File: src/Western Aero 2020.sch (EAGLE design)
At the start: 97 parts, among them IC1 LT1963AET, IC2 LT1963AET, J1 PITOT, J10 ANA_IO, J11 PWR, J2 BUZZER, J3 RX2/TX2, J4 RX3/TX3, J5 SPI, J6 DIG_IO, J7 RX1/TX1, J8 DIG_IO, J9 REF/GND, U3 TEENSY_3.5_DIL+4, U5 SPARKFUN_MPU9250_IMU, U6 ADAFRUIT_MPL3115A2_BAROMETER, U7 ADAFRUIT_INA219_BATTERY_SENSOR, U8 ADAFRUIT_RFM95W_LORA_RADIO, U9 ADAFRUIT_MTK3339_GPS

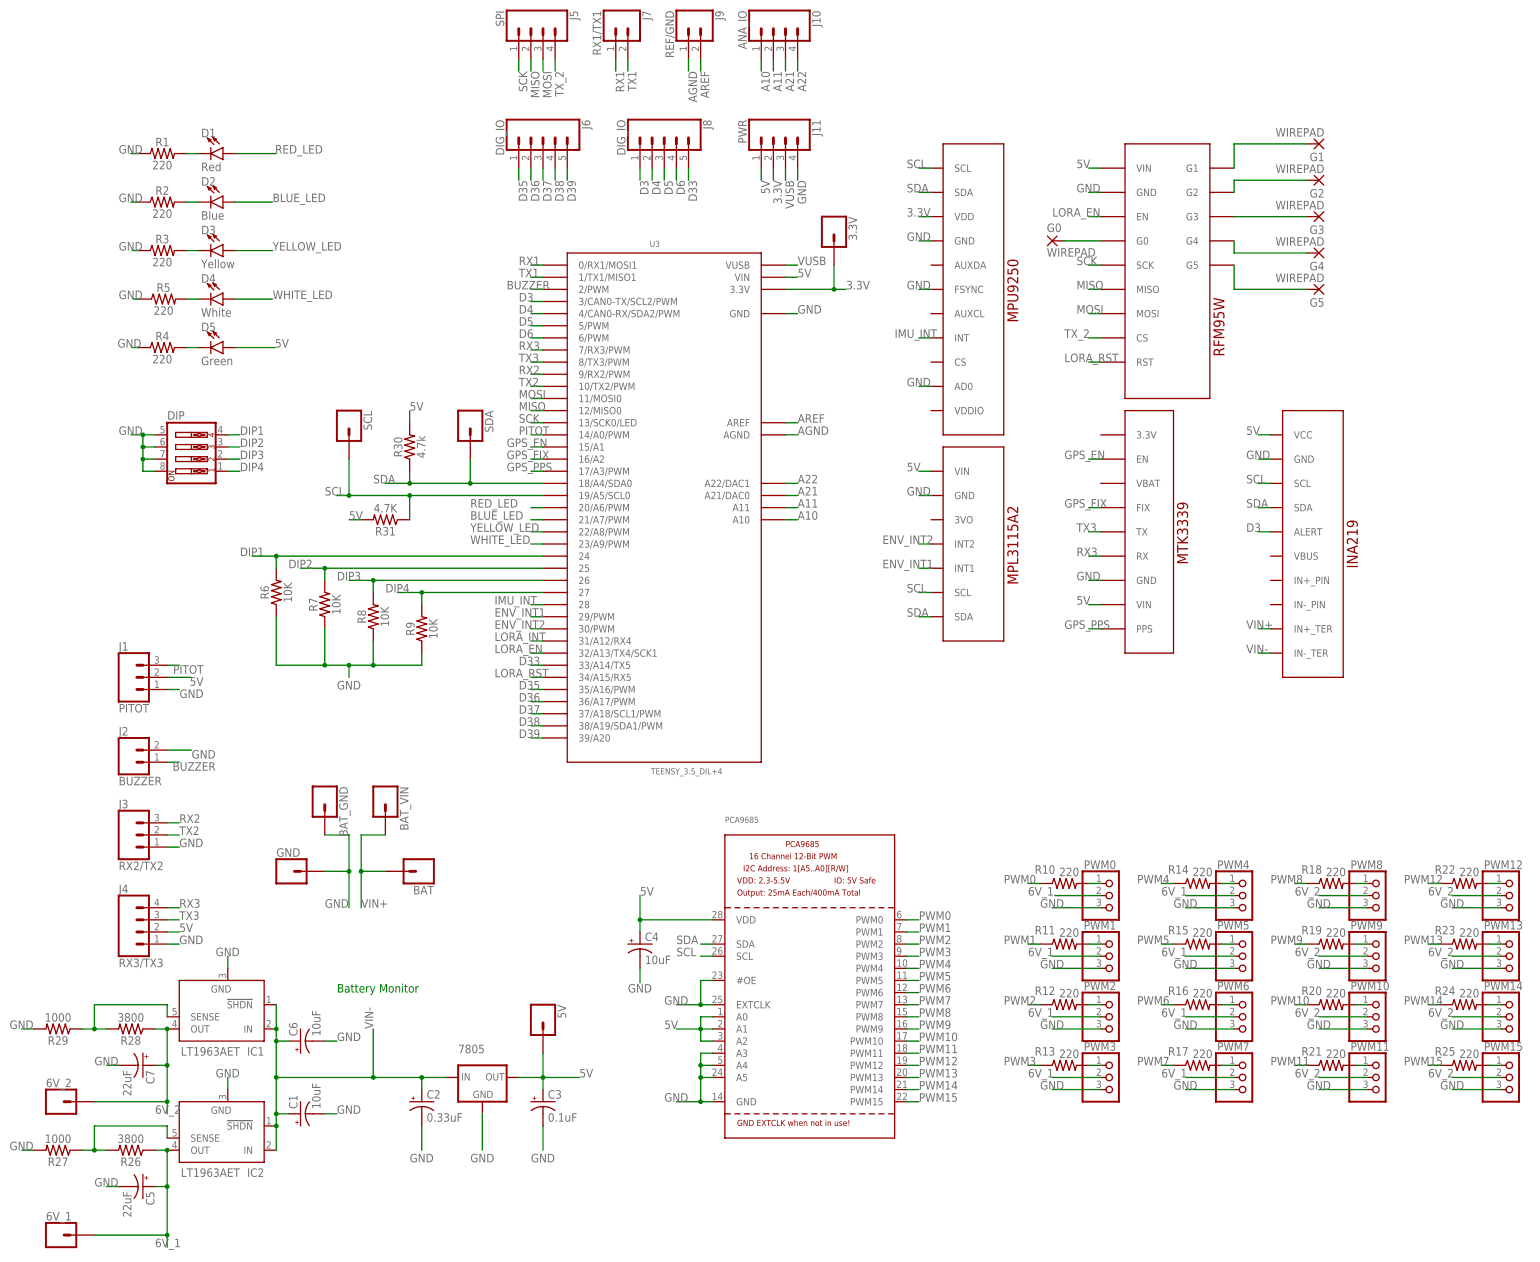
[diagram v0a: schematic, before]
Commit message: Remove battery monitor
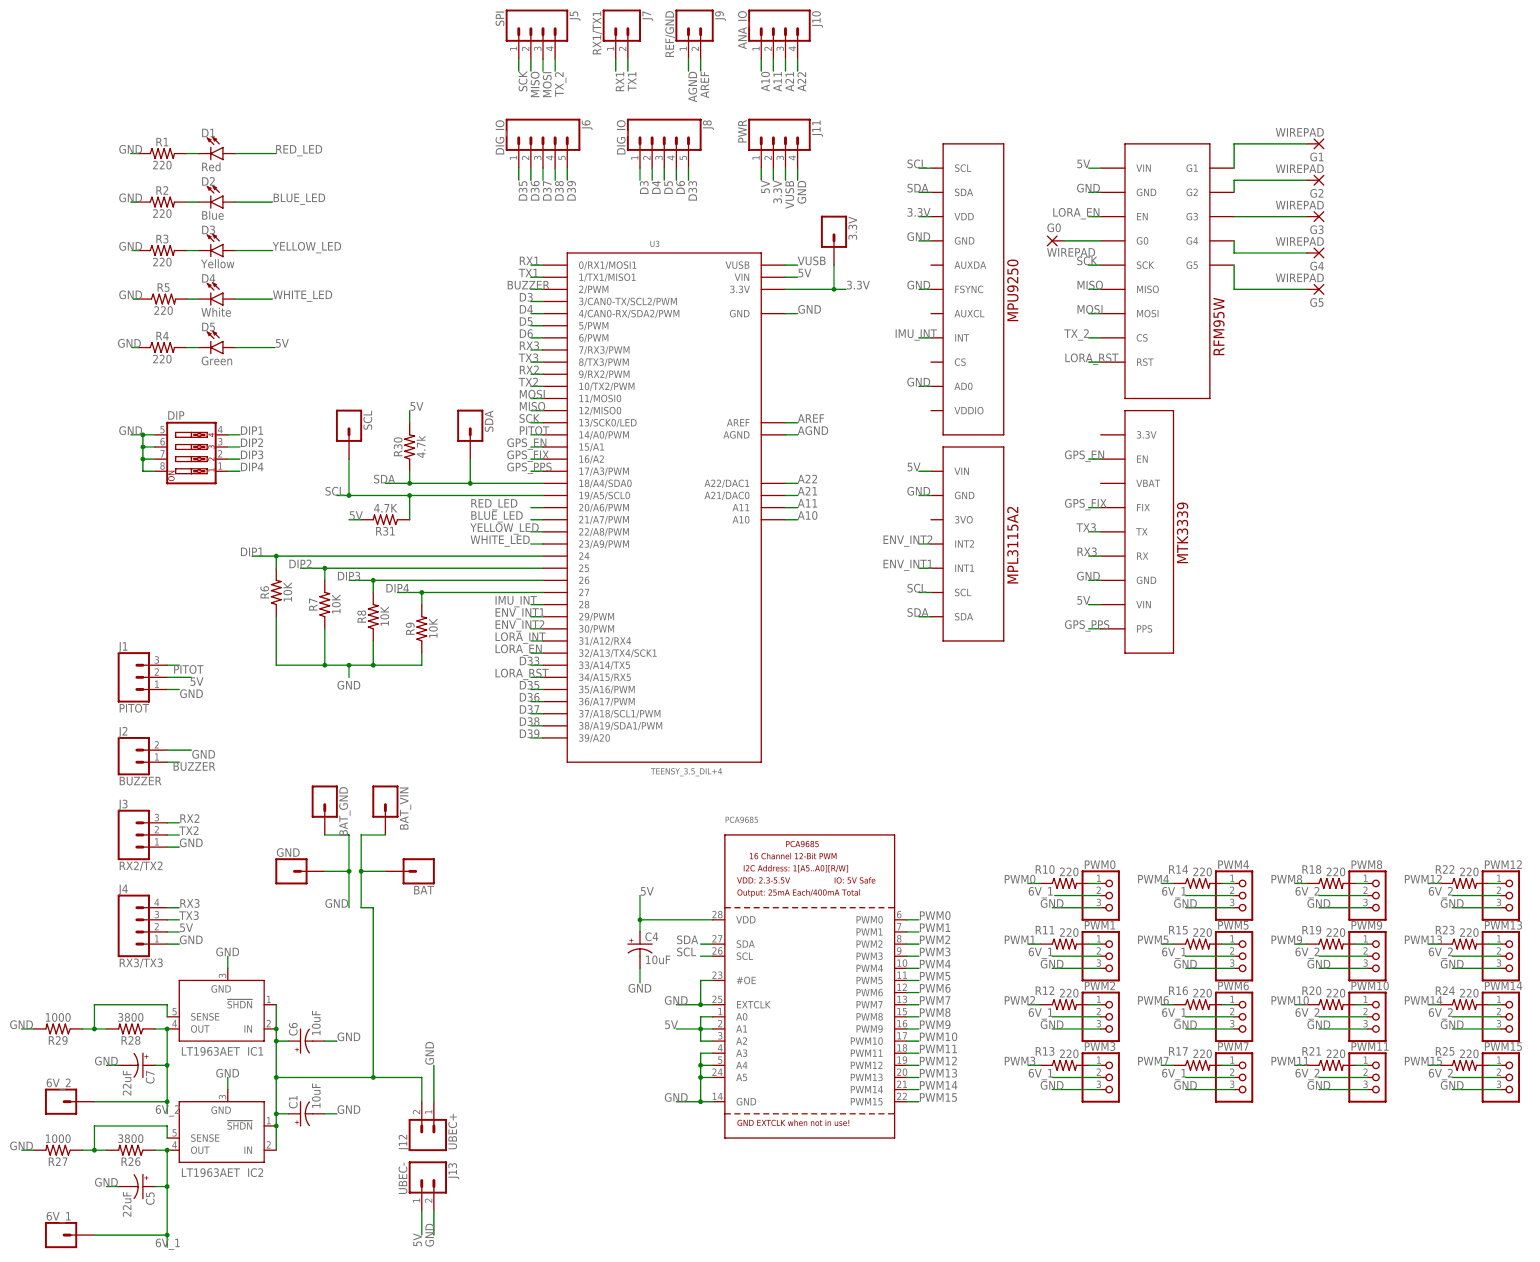
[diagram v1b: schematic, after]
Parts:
- removed 5V: (no value), SparkFun-Connectors:CONN_01
- removed 7805: 7805, SparkFun-IC-Power:V_REG_78XXSINK
- removed C2: 0.33uF, SparkFun-Capacitors:10UF-POLAR-RADIAL-2.5MM-25V-20%
- removed C3: 0.1uF, SparkFun-Capacitors:10UF-POLAR-RADIAL-2.5MM-25V-20%
- removed U7: ADAFRUIT_INA219_BATTERY_SENSOR, AERO_Eagle_Library:ADAFRUIT_INA219_BATTERY_SENSOR
- added J12: UBEC+, SparkFun-Connectors:CONN_02
- added J13: UBEC-, SparkFun-Connectors:CONN_02
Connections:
- removed net VIN+: BAT.1, BAT_VIN.1, U7.IN+_TER
- removed net VIN-: 7805.IN, C1.+, C2.+, C6.+, IC1.!SHDN, IC1.IN, IC2.!SHDN, IC2.IN, U7.IN-_TER
- new net BAT+: BAT.1, BAT_VIN.1, C1.+, C6.+, IC1.!SHDN, IC1.IN, IC2.!SHDN, IC2.IN, J12.2
- net 5V: now also J13.1; no longer 5V.1, 7805.OUT, C3.+, U7.VCC
- net D3: no longer U7.ALERT
- net GND: now also J12.1, J13.2; no longer 7805.GND, C2.-, C3.-, U7.GND
- net SCL: no longer U7.SCL
- net SDA: no longer U7.SDA
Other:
- note removed: "Battery Monitor"

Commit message: UBEC now supplies 6v with a 5v reg for onboard systems
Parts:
- removed 6V_1, 6V_2: (no value), SparkFun-Connectors:CONN_01
- removed C5, C7: 22uF, SparkFun-Capacitors:10UF-POLAR-RADIAL-2.5MM-25V-20%
- removed C6: 10uF, SparkFun-Capacitors:10UF-POLAR-RADIAL-2.5MM-25V-20%
- removed IC1, IC2: LT1963AET, linear-technology:LT1963AET
- removed J12: UBEC+, SparkFun-Connectors:CONN_02
- removed J13: UBEC-, SparkFun-Connectors:CONN_02
- removed R26, R28: 3800, SparkFun-Resistors:330OHM-HORIZ-1/10W-5%
- removed R27, R29: 1000, SparkFun-Resistors:330OHM-HORIZ-1/10W-5%
- added 5V: (no value), SparkFun-Connectors:CONN_01
- added C2: 22uF, SparkFun-Capacitors:10UF-POLAR-RADIAL-2.5MM-25V-20%
- added U1: (no value), SparkFun-IC-Power:V_REG_78XXSINK
- C1: value 10uF -> 0.47uF
- renumbered BAT to 6V, BAT_GND to UBEC_GND, BAT_VIN to UBEC_VIN
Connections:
- removed net 6V_1: 6V_1.1, C5.+, IC2.OUT, JP1.2, JP2.2, JP3.2, JP4.2, JP5.2, JP6.2, JP7.2, JP8.2, R26.1
- removed net 6V_2: 6V_2.1, C7.+, IC1.OUT, JP10.2, JP11.2, JP12.2, JP13.2, JP14.2, JP15.2, JP16.2, JP9.2, R28.1
- removed net BAT+: 6V.1, C1.+, C6.+, IC1.!SHDN, IC1.IN, IC2.!SHDN, IC2.IN, J12.2, UBEC_VIN.1
- removed net N$28: IC1.SENSE, R28.2, R29.1
- removed net N$29: IC2.SENSE, R26.2, R27.1
- new net 6V: 6V.1, C1.+, JP1.2, JP10.2, JP11.2, JP12.2, JP13.2, JP14.2, JP15.2, JP16.2, JP2.2, JP3.2, JP4.2, JP5.2, JP6.2, JP7.2, JP8.2, JP9.2, U1.IN, UBEC_VIN.1
- net 5V: now also 5V.1, C2.+, U1.OUT; no longer J13.1
- net GND: now also C2.-; no longer C5.-, C6.-, C7.-, IC1.GND, IC2.GND, J12.1, J13.2, R27.2, R29.2
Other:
- moved on the sheet: C1
